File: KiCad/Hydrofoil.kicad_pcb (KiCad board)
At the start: 2 copper layers, 219.6 x 35 mm, 20 parts, among them J1 Conn_01x05_Pin, U1 LM334M, U2 LM334M, U3 ADS1115IDGS

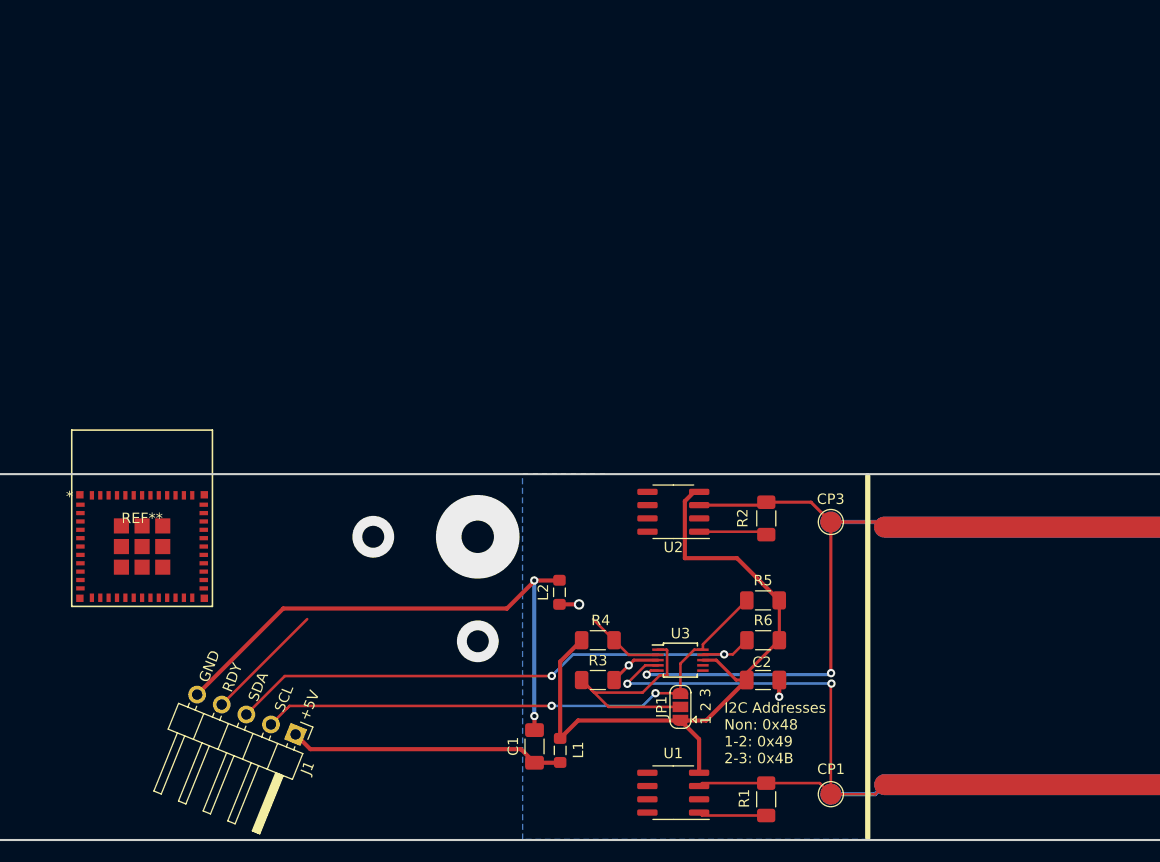
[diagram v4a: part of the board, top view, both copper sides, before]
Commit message: Add level shifters
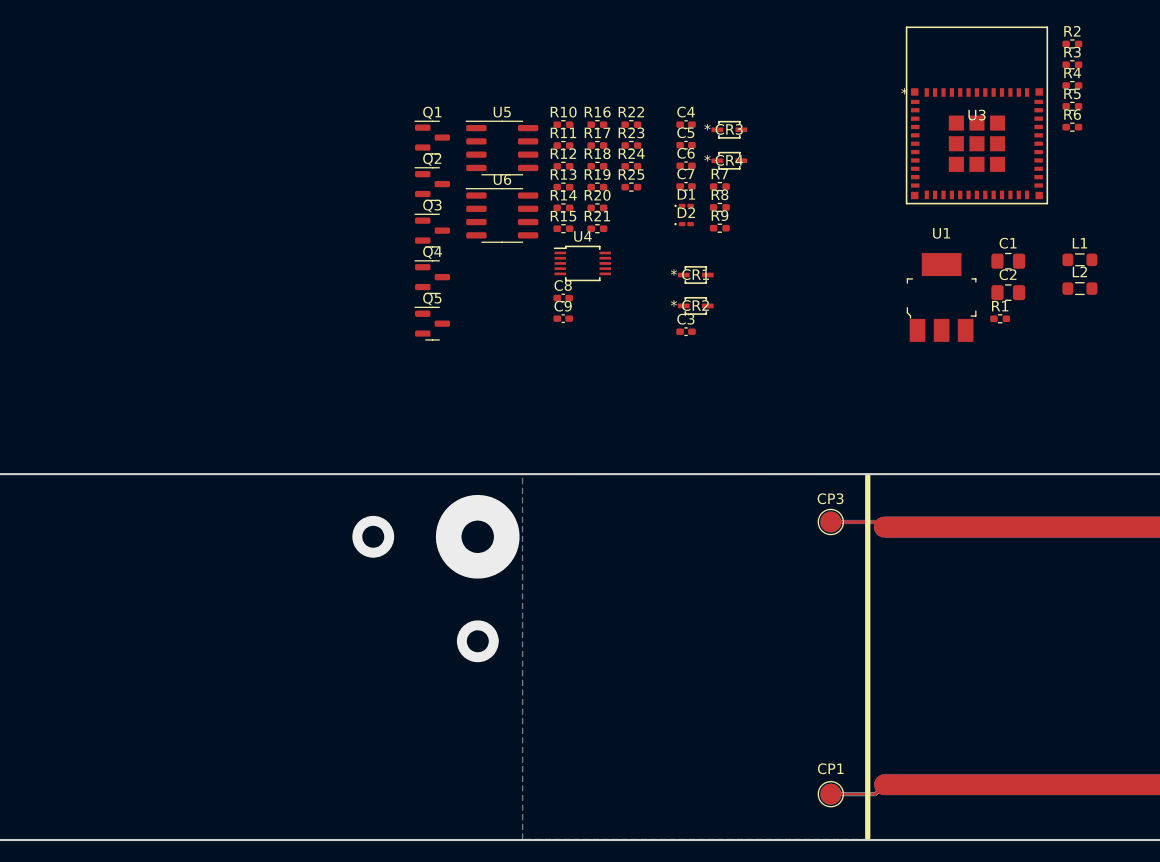
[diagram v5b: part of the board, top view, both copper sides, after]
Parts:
- removed J1: Conn_01x05_Pin, Connector_PinHeader_2.54mm:PinHeader_1x05_P2.54mm_Horizontal
- removed JP1: SolderJumper_3_Open, Jumper:SolderJumper-3_P1.3mm_Open_RoundedPad1.0x1.5mm
- removed REF**: ESP32-C3-MINI-1_EXP, ESP32-C3-MINI-1-N4:ESP32-C3-MINI-1_EXP
- removed U2: LM334M, Package_SO:SOIC-8_3.9x4.9mm_P1.27mm
- added C3: 1u, Capacitor_SMD:C_0402_1005Metric_Pad0.74x0.62mm_HandSolder, F.Cu at (116.8, 57.2)
- added C4: 1u, Capacitor_SMD:C_0402_1005Metric_Pad0.74x0.62mm_HandSolder, F.Cu at (116.8, 37.4)
- added C5: 1u, Capacitor_SMD:C_0402_1005Metric_Pad0.74x0.62mm_HandSolder, F.Cu at (116.8, 39.4)
- added C6: 1u, Capacitor_SMD:C_0402_1005Metric_Pad0.74x0.62mm_HandSolder, F.Cu at (116.8, 41.4)
- added C7: 1u, Capacitor_SMD:C_0402_1005Metric_Pad0.74x0.62mm_HandSolder, F.Cu at (116.8, 43.3)
- added C8: 1u, Capacitor_SMD:C_0402_1005Metric_Pad0.74x0.62mm_HandSolder, F.Cu at (105.0, 54.0)
- added C9: 1u, Capacitor_SMD:C_0402_1005Metric_Pad0.74x0.62mm_HandSolder, F.Cu at (105.0, 56.0)
- added CR1: CUS08F30_H3FT, CUS08F30:USC_TOS, F.Cu at (117.7, 51.8)
- added CR2: CUS08F30_H3FT, CUS08F30:USC_TOS, F.Cu at (117.7, 54.8)
- added CR3: CUS08F30_H3FT, CUS08F30:USC_TOS, F.Cu at (120.9, 37.9)
- added CR4: CUS08F30_H3FT, CUS08F30:USC_TOS, F.Cu at (120.9, 40.9)
- added D1: Green, LED_SMD:LED_0201_0603Metric_Pad0.64x0.40mm_HandSolder, F.Cu at (116.8, 45.2)
- added D2: Red, LED_SMD:LED_0201_0603Metric_Pad0.64x0.40mm_HandSolder, F.Cu at (116.8, 46.9)
- added Q1: BSS138, Package_TO_SOT_SMD:SOT-23, F.Cu at (92.5, 38.7)
- added Q2: BSS138, Package_TO_SOT_SMD:SOT-23, F.Cu at (92.5, 43.1)
- added Q3: BSS138, Package_TO_SOT_SMD:SOT-23, F.Cu at (92.5, 47.6)
- added Q4: BSS138, Package_TO_SOT_SMD:SOT-23, F.Cu at (92.5, 52.0)
- added Q5: BSS138, Package_TO_SOT_SMD:SOT-23, F.Cu at (92.5, 56.5)
- added R10: 10.5, Resistor_SMD:R_0402_1005Metric_Pad0.72x0.64mm_HandSolder, F.Cu at (105.0, 37.4)
- added R11: 10.5k, Resistor_SMD:R_0402_1005Metric_Pad0.72x0.64mm_HandSolder, F.Cu at (105.0, 39.4)
- added R12: 10.5k, Resistor_SMD:R_0402_1005Metric_Pad0.72x0.64mm_HandSolder, F.Cu at (105.0, 41.4)
- added R13: 10.5k, Resistor_SMD:R_0402_1005Metric_Pad0.72x0.64mm_HandSolder, F.Cu at (105.0, 43.4)
- added R14: 150R, Resistor_SMD:R_0402_1005Metric_Pad0.72x0.64mm_HandSolder, F.Cu at (105.0, 45.4)
- added R15: 10.5k, Resistor_SMD:R_0402_1005Metric_Pad0.72x0.64mm_HandSolder, F.Cu at (105.0, 47.4)
- added R16: 10.5k, Resistor_SMD:R_0402_1005Metric_Pad0.72x0.64mm_HandSolder, F.Cu at (108.3, 37.4)
- added R17: 150R, Resistor_SMD:R_0402_1005Metric_Pad0.72x0.64mm_HandSolder, F.Cu at (108.3, 39.4)
- added R18: 10.5k, Resistor_SMD:R_0402_1005Metric_Pad0.72x0.64mm_HandSolder, F.Cu at (108.3, 41.4)
- added R19: 10.5k, Resistor_SMD:R_0402_1005Metric_Pad0.72x0.64mm_HandSolder, F.Cu at (108.3, 43.4)
- added R20: 10.5k, Resistor_SMD:R_0402_1005Metric_Pad0.72x0.64mm_HandSolder, F.Cu at (108.3, 45.4)
- added R21: 10.5k, Resistor_SMD:R_0402_1005Metric_Pad0.72x0.64mm_HandSolder, F.Cu at (108.3, 47.4)
- added R22: 10.5k, Resistor_SMD:R_0402_1005Metric_Pad0.72x0.64mm_HandSolder, F.Cu at (111.5, 37.4)
- added R23: 10.5k, Resistor_SMD:R_0402_1005Metric_Pad0.72x0.64mm_HandSolder, F.Cu at (111.5, 39.4)
- added R24: 10.5k, Resistor_SMD:R_0402_1005Metric_Pad0.72x0.64mm_HandSolder, F.Cu at (111.5, 41.4)
- added R25: 10.5k, Resistor_SMD:R_0402_1005Metric_Pad0.72x0.64mm_HandSolder, F.Cu at (111.5, 43.4)
- added R7: 10.5k, Resistor_SMD:R_0402_1005Metric_Pad0.72x0.64mm_HandSolder, F.Cu at (120.0, 43.3)
- added R8: 1k, Resistor_SMD:R_0402_1005Metric_Pad0.72x0.64mm_HandSolder, F.Cu at (120.0, 45.3)
- added R9: 1k, Resistor_SMD:R_0402_1005Metric_Pad0.72x0.64mm_HandSolder, F.Cu at (120.0, 47.3)
- added U4: ADS1115IDGS, Package_SO:TSSOP-10_3x3mm_P0.5mm, F.Cu at (106.9, 50.7)
- added U5: LM334M, Package_SO:SOIC-8_3.9x4.9mm_P1.27mm, F.Cu at (99.2, 39.7)
- added U6: LM334M, Package_SO:SOIC-8_3.9x4.9mm_P1.27mm, F.Cu at (99.2, 46.1)
- C1, C2: value 1uF -> 10u; footprint Capacitor_SMD:C_1206_3216Metric_Pad1.33x1.80mm_HandSolder -> Capacitor_SMD:C_0805_2012Metric_Pad1.18x1.45mm_HandSolder
- R1, R2: value 150R -> 10.5k; footprint Resistor_SMD:R_1206_3216Metric_Pad1.30x1.75mm_HandSolder -> Resistor_SMD:R_0402_1005Metric_Pad0.72x0.64mm_HandSolder
- R3, R4: value 10k -> 1k; footprint Resistor_SMD:R_1206_3216Metric_Pad1.30x1.75mm_HandSolder -> Resistor_SMD:R_0402_1005Metric_Pad0.72x0.64mm_HandSolder
- R5, R6: value 10k -> 10.5k; footprint Resistor_SMD:R_1206_3216Metric_Pad1.30x1.75mm_HandSolder -> Resistor_SMD:R_0402_1005Metric_Pad0.72x0.64mm_HandSolder
- U1: value LM334M -> LD1117S33CTR; footprint Package_SO:SOIC-8_3.9x4.9mm_P1.27mm -> digikey-footprints:SOT-223
- U3: value ADS1115IDGS -> ESP32-C3-MINI-1-N4; footprint Package_SO:TSSOP-10_3x3mm_P0.5mm -> ESP32-C3-MINI-1-N4:ESP32-C3-MINI-1_EXP
- moved R3 74.3 mm to (153.7, 31.7)
- moved R4 69.8 mm to (153.7, 33.7)
- moved L1 68.4 mm to (154.4, 50.3), turned to 0 degrees
- moved C1 64.9 mm to (147.6, 50.5), turned to 0 degrees
- moved U3 59.3 mm to (144.6, 36.5)
- moved L2 57.6 mm to (154.4, 53.1), turned to 0 degrees
- moved R6 57.3 mm to (153.7, 37.7), turned to 0 degrees
- moved R5 55.8 mm to (153.7, 35.7), turned to 0 degrees
- moved R2 54.0 mm to (153.7, 29.7), turned to 0 degrees
- moved U1 53.9 mm to (141.2, 53.9), turned to 0 degrees
- moved R1 51.1 mm to (146.8, 56.0), turned to 0 degrees
- moved C2 43.9 mm to (147.6, 53.5), turned to 0 degrees
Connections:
- C1 pad 1: /+5Vraw -> /+5V-Logic
- C1 pad 2: /GNDraw -> GND
- C2 pad 1: GND -> +3.3V
- C2 pad 2: +5V -> GND
- CP2 pad 1: GND -> GNDA
- CP4 pad 1: GND -> GNDA
- L1 pad 1: +5V -> +5VA
- L1 pad 2: /+5Vraw -> +5V
- L2 pad 1: GND -> GNDA
- L2 pad 2: /GNDraw -> GND
- R1 pad 1: /SETcur1 -> /+5V-Raw
- R1 pad 2: AIN0 -> Net-(U2-EN)
- R2 pad 1: /SETcur2 -> +3.3V
- R2 pad 2: AIN1 -> Net-(U3-EN)
- R3 pad 1: /ADDR -> +3.3V
- R3 pad 2: GND -> Net-(D1-A)
- R4 pad 1: +5V -> +3.3V
- R4 pad 2: RDY -> Net-(D2-A)
- R5 pad 1: +5V -> +3.3V
- R5 pad 2: SCL -> User-LED
- R6 pad 1: +5V -> +3.3V
- R6 pad 2: SDA -> Input-Boot
- U1 pad 1: /SETcur1 -> GND
- U1 pad 2: AIN0 -> +3.3V
- U1 pad 3: AIN0 -> /+5V-Logic
- U1 pad 4: +5V -> +3.3V
- U3 pad 1: /ADDR -> GND
- U3 pad 10: SCL -> unconnected-(U3-NC-Pad10)
- U3 pad 2: RDY -> GND
- U3 pad 3: GND -> +3.3V
- U3 pad 4: AIN0 -> unconnected-(U3-NC-Pad4)
- U3 pad 5: AIN1 -> Input-Boot
- U3 pad 8: +5V -> Net-(U3-EN)
- U3 pad 9: SDA -> unconnected-(U3-NC-Pad9)
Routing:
- net GND: track 218.3 -> 0.00 mm, vias 3 -> 0
- net GNDA: track 0.00 -> 209.8 mm
- net +5V: track 67.9 -> 0.00 mm
- net /GNDraw: track 54.1 -> 0.00 mm, vias 2 -> 0
- net SDA: track 52.9 -> 0.00 mm, vias 2 -> 0
- net SCL: track 52.4 -> 0.00 mm, vias 2 -> 0
- net AIN0: track 164.5 -> 117.5 mm, vias 2 -> 0
- net AIN1: track 139.2 -> 92.3 mm, vias 2 -> 0
- net /+5Vraw: track 26.4 -> 0.00 mm
- net /ADDR: track 23.2 -> 0.00 mm
- net RDY: track 19.2 -> 0.00 mm
- net /SETcur2: track 6.53 -> 0.00 mm
- net /SETcur1: track 6.53 -> 0.00 mm
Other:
- board text removed: "+5V"
- board text removed: "1"
- board text removed: "2"
- board text removed: "3"
- board text removed: "GND"
- board text removed: "I2C Addresses Non: 0x48 1-2: 0x49 2-3: 0x4B"
- board text removed: "RDY"
- board text removed: "SCL"
- board text removed: "SDA"

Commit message: Change resistor values
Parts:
- added TP3: ~, Connector:Tag-Connect_TC2030-IDC-NL_2x03_P1.27mm_Vertical, F.Cu at (82.1, 38.9)
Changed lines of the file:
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@@
   (net 61 "unconnected-(U4-AIN2-Pad6)")
   (net 62 "unconnected-(U4-AIN3-Pad7)")
+  (net 63 "ESP-En")
   (footprint "LED_SMD:LED_0201_0603Metric_Pad0.64x0.40mm_HandSolder" (layer "F.Cu")
     (at 116.797876 46.93204)
@@
     )
   )
+  (footprint "Connector:Tag-Connect_TC2030-IDC-NL_2x03_P1.27mm_Vertical" (layer "F.Cu")
+    (at 82.118333 38.874349)
+    (descr "Tag-Connect programming header; http://www.tag-connect.com/Materials/TC2030-IDC-NL.pdf")
+    (tags "tag connect programming header pogo pins")
+    (property "Sheetfile" "ESP32-C3-MINI-1-N4.kicad_sch")
+    (property "Sheetname" "ESP32-C3-MINI-1-N4")
+    (attr exclude_from_pos_files)
+    (fp_text reference "TP3" (at 0 2.7) (layer "F.SilkS")
+        (effects (font (size 1 1) (thickness 0.15)))
+    )
+    (fp_text value "~" (at 0 -2.3) (layer "F.Fab")
+        (effects (font (size 1 1) (thickness 0.15)))
+    )
+    (fp_text user "KEEPOUT" (at 0 0) (layer "Cmts.User")
+        (effects (font (size 0.4 0.4) (thickness 0.07)))
+    )
+    (fp_text user "${REFERENCE}" (at 0 0) (layer "F.Fab")
+        (effects (font (size 1 1) (thickness 0.15)))
+    )
+    (fp_line (start -1.905 1.27) (end -1.905 0.635)
+      (stroke (width 0.12) (type solid)) (layer "F.SilkS"))
+    (fp_line (start -1.27 1.27) (end -1.905 1.27)
+      (stroke (width 0.12) (type solid)) (layer "F.SilkS"))
+    (fp_line (start -3.5 -2) (end 3.5 -2)
+      (stroke (width 0.05) (type solid)) (layer "F.CrtYd"))
+    (fp_line (start -3.5 2) (end -3.5 -2)
+      (stroke (width 0.05) (type solid)) (layer "F.CrtYd"))
+    (fp_line (start 3.5 -2) (end 3.5 2)
+      (stroke (width 0.05) (type solid)) (layer "F.CrtYd"))
+    (fp_line (start 3.5 2) (end -3.5 2)
+      (stroke (width 0.05) (type solid)) (layer "F.CrtYd"))
+    (pad "" np_thru_hole circle (at -2.54 0) (size 0.9906 0.9906) (drill 0.9906) (layers "*.Cu" "*.Mask"))
+    (pad "" np_thru_hole circle (at 2.54 -1.016) (size 0.9906 0.9906) (drill 0.9906) (layers "*.Cu" "*.Mask"))
+    (pad "" np_thru_hole circle (at 2.54 1.016) (size 0.9906 0.9906) (drill 0.9906) (layers "*.Cu" "*.Mask"))
+    (pad "1" connect circle (at -1.27 0.635) (size 0.7874 0.7874) (layers "F.Cu" "F.Mask")
+      (net 63 "ESP-En") (pintype "input"))
+    (pad "2" connect circle (at -1.27 -0.635) (size 0.7874 0.7874) (layers "F.Cu" "F.Mask")
+      (net 12 "+5V-Prog") (pintype "power_in"))
+    (pad "3" connect circle (at 0 0.635) (size 0.7874 0.7874) (layers "F.Cu" "F.Mask")
+      (net 56 "ESP-Tx") (pintype "input"))
+    (pad "4" connect circle (at 0 -0.635) (size 0.7874 0.7874) (layers "F.Cu" "F.Mask")
+      (net 3 "GND") (pintype "power_in"))
+    (pad "5" connect circle (at 1.27 0.635) (size 0.7874 0.7874) (layers "F.Cu" "F.Mask")
+      (net 55 "ESP-Rx") (pintype "input"))
+    (pad "6" connect circle (at 1.27 -0.635) (size 0.7874 0.7874) (layers "F.Cu" "F.Mask")
+      (net 14 "ESP-Boot") (pintype "output"))
+    (zone (net 0) (net_name "") (layer "F.Cu") (hatch full 0.508)
+      (connect_pads (clearance 0))
+      (min_thickness 0.254) (filled_areas_thickness no)
+      (keepout (tracks allowed) (vias not_allowed) (pads allowed) (copperpour not_allowed) (footprints not_allowed))
+      (fill (thermal_gap 0.508) (thermal_bridge_width 0.508))
+      (polygon
+        (pts
+          (xy 83.388333 38.239349)
+          (xy 80.848333 38.239349)
+          (xy 80.848333 39.509349)
+          (xy 83.388333 39.509349)
+        )
+      )
+    )
+  )
   (footprint "Resistor_SMD:R_0402_1005Metric_Pad0.72x0.64mm_HandSolder" (layer "F.Cu")
     (at 153.723374 31.686694)
@@
         (effects (font (size 1 1) (thickness 0.15)))
     )
+    (fp_text user "*" (at -6.9414 -2.0759 unlocked) (layer "F.SilkS")
+        (effects (font (size 1 1) (thickness 0.15)))
+    )
     (fp_text user "*" (at -6.9414 -2.0759) (layer "F.SilkS")
         (effects (font (size 1 1) (thickness 0.15)))
     )
-    (fp_text user "*" (at -6.9414 -2.0759 unlocked) (layer "F.SilkS")
+    (fp_text user "*" (at -5.2396 -1.6949 unlocked) (layer "F.Fab")
         (effects (font (size 1 1) (thickness 0.15)))
     )
@@
         (effects (font (size 1 1) (thickness 0.15)))
     )
-    (fp_text user "*" (at -5.2396 -1.6949 unlocked) (layer "F.Fab")
-        (effects (font (size 1 1) (thickness 0.15)))
-    )

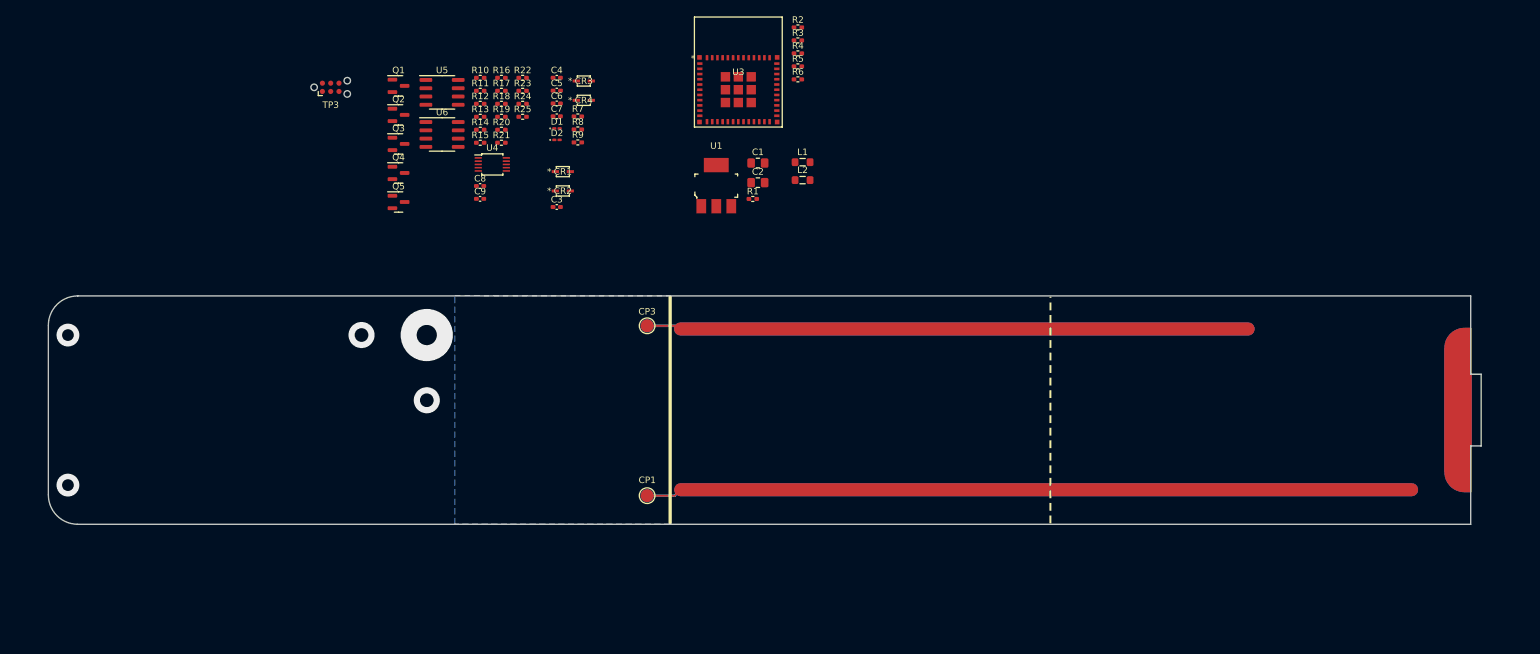
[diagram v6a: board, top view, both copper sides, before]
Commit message: Change reverse polarity protection, start the PCB design
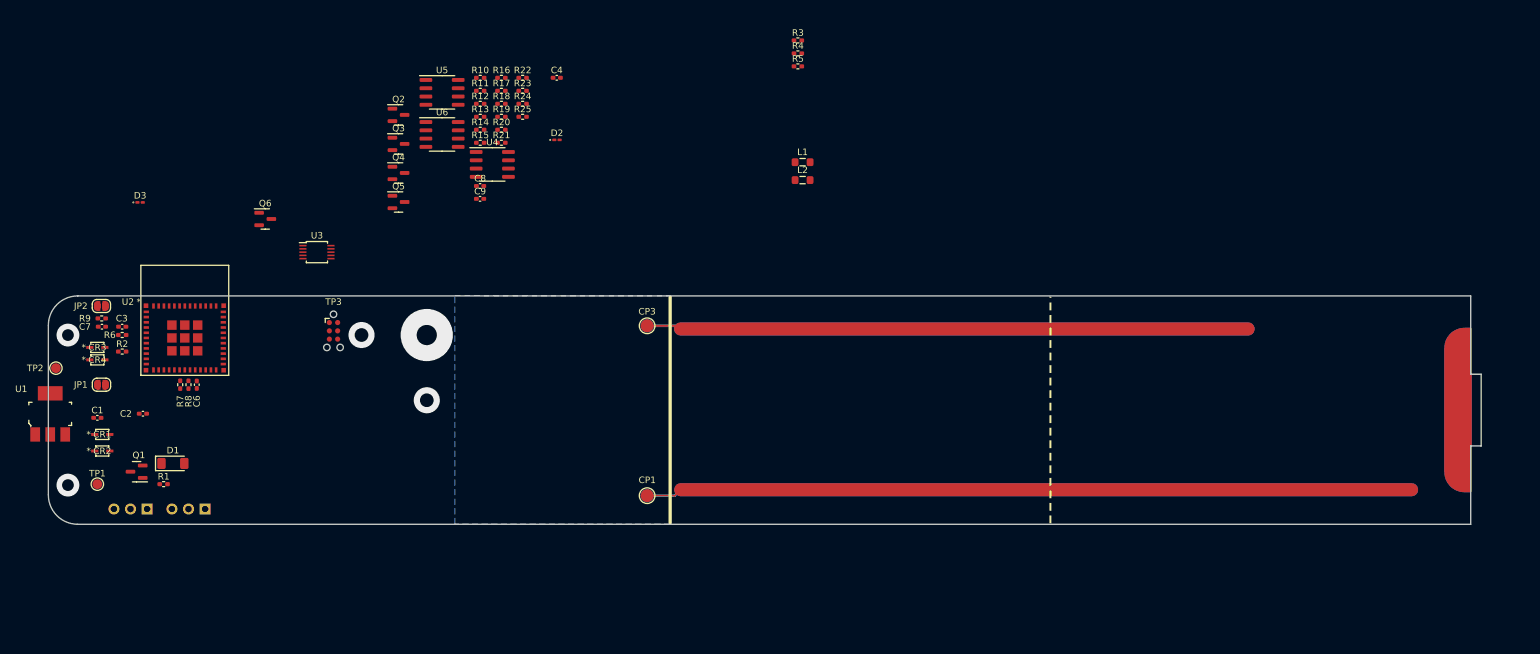
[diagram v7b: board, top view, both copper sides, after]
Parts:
- removed C5: 1u, Capacitor_SMD:C_0402_1005Metric_Pad0.74x0.62mm_HandSolder
- added D3: Red, LED_SMD:LED_0201_0603Metric_Pad0.64x0.40mm_HandSolder, F.Cu at (52.9, 56.5)
- added J1: Conn_01x03_Pin, Custom_Footprints:Solder_Connector, F.Cu at (51.4, 103.5)
- added J2: Conn_01x03_Pin, Custom_Footprints:Solder_Connector, F.Cu at (60.3, 103.5)
- added JP1: Jumper_2_Open, Jumper:SolderJumper-2_P1.3mm_Open_RoundedPad1.0x1.5mm, F.Cu at (47.0, 84.5)
- added JP2: Jumper_2_Open, Jumper:SolderJumper-2_P1.3mm_Open_RoundedPad1.0x1.5mm, F.Cu at (47.0, 72.4)
- added Q6: BSS138, Package_TO_SOT_SMD:SOT-23, F.Cu at (72.1, 59.1)
- added TP1: TestPoint, TestPoint:TestPoint_Pad_D1.5mm, F.Cu at (46.4, 99.7)
- added TP2: TestPoint, TestPoint:TestPoint_Pad_D1.5mm, F.Cu at (40.0, 81.9)
- added U2: ESP32-C3-MINI-1-N4, ESP32-C3-MINI-1-N4:ESP32-C3-MINI-1_EXP, F.Cu at (59.8, 74.6)
- C1, C2: footprint Capacitor_SMD:C_0805_2012Metric_Pad1.18x1.45mm_HandSolder -> Capacitor_SMD:C_0402_1005Metric_Pad0.74x0.62mm_HandSolder
- C3: value 1u -> 10u
- D1: value Green -> BZV55B7V5; footprint LED_SMD:LED_0201_0603Metric_Pad0.64x0.40mm_HandSolder -> Diode_SMD:D_MiniMELF
- D2: value Red -> Green
- Q1: value BSS138 -> AO3413
- R1: value 10.5k -> 100k
- R10: value 10.5 -> 10k
- R11, R12, R13, R15, R16, R18, R19, R2, R20, R21, R22, R23, R24, R25, R5, R6, R7: value 10.5k -> 10k
- U3: value ESP32-C3-MINI-1-N4 -> ADS1115IDGS; footprint ESP32-C3-MINI-1-N4:ESP32-C3-MINI-1_EXP -> Package_SO:TSSOP-10_3x3mm_P0.5mm
- U4: value ADS1115IDGS -> LM334M; footprint Package_SO:TSSOP-10_3x3mm_P0.5mm -> Package_SO:SOIC-8_3.9x4.9mm_P1.27mm
- moved R2 114.9 mm to (50.2, 79.4)
- moved R6 110.7 mm to (50.2, 76.8)
- moved C1 108.5 mm to (46.4, 89.5)
- moved U1 107.9 mm to (39.1, 88.9)
- moved C2 100.7 mm to (53.3, 88.9)
- moved R1 100.3 mm to (56.5, 99.7)
- moved CR3 85.0 mm to (46.4, 78.7)
- moved CR4 84.5 mm to (46.4, 80.6)
- moved CR1 81.3 mm to (47.1, 92.1)
- moved CR2 81.1 mm to (47.1, 94.6)
- moved D1 78.1 mm to (57.9, 96.5)
- moved R9 77.8 mm to (47.0, 74.3)
- moved C7 76.8 mm to (47.1, 75.6)
- moved R7 73.5 mm to (59.1, 84.5), turned to 90 degrees
- moved Q1 71.5 mm to (52.4, 97.8), turned to 180 degrees
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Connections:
- C2 pad 1: +3.3V -> +5V
- C3 pad 1: +5V -> +3.3V
- C4 pad 1: Net-(U3-EN) -> Net-(U2-EN)
- D1 pad 1: GND -> +5V
- D2 pad 1: User-LED -> GND
- Q1 pad 1: +3.3V -> Net-(D1-A)
- Q1 pad 2: Ready-LV -> +5V
- Q1 pad 3: Ready-HV -> /+5V-Raw
- Q2 pad 2: SDA-LV -> Ready-LV
- Q2 pad 3: SDA-HV -> Ready-HV
- Q3 pad 2: SCL-LV -> SDA-LV
- Q3 pad 3: SCL-HV -> SDA-HV
- Q4 pad 2: PWM-In-LV -> SCL-LV
- Q4 pad 3: PWM-In-HV -> SCL-HV
- Q5 pad 2: PWM-Out-LV -> PWM-In-LV
- Q5 pad 3: PWM-Out-HV -> PWM-In-HV
- R1 pad 1: /+5V-Raw -> Net-(D1-A)
- R1 pad 2: Net-(U2-EN) -> GND
- R10 pad 1: Net-(U4-ADDR) -> Net-(U3-ADDR)
- R15 pad 1: +3.3V -> unconnected-(R15-Pad1)
- R15 pad 2: Ready-LV -> unconnected-(R15-Pad2)
- R16 pad 2: SDA-LV -> Ready-LV
- R2 pad 2: Net-(U3-EN) -> Net-(U2-EN)
- R3 pad 2: Net-(D1-A) -> Net-(D2-A)
- R4 pad 2: Net-(D2-A) -> Net-(D3-A)
- U3 pad 1: GND -> Net-(U3-ADDR)
- U3 pad 10: unconnected-(U3-NC-Pad10) -> SCL-HV
- U3 pad 2: GND -> Ready-HV
- U3 pad 3: +3.3V -> GNDA
- U3 pad 4: unconnected-(U3-NC-Pad4) -> AIN0
- U3 pad 5: Input-Boot -> AIN1
- U3 pad 8: Net-(U3-EN) -> +5VA
- U3 pad 9: unconnected-(U3-NC-Pad9) -> SDA-HV
- U4 pad 1: Net-(U4-ADDR) -> /ADS1115-ADC/SETcur1
- U4 pad 2: Ready-HV -> AIN0
- U4 pad 3: GNDA -> AIN0
- U4 pad 4: AIN0 -> +5VA
- U4 pad 5: AIN1 -> (no net)
- U4 pad 6: unconnected-(U4-AIN2-Pad6) -> AIN0
- U4 pad 7: unconnected-(U4-AIN3-Pad7) -> AIN0
- U4 pad 8: +5VA -> (no net)
- U5 pad 1: /ADS1115-ADC/SETcur1 -> /ADS1115-ADC/SETcur2
- U5 pad 2: AIN0 -> AIN1
- U5 pad 3: AIN0 -> AIN1
- U5 pad 6: AIN0 -> AIN1
- U5 pad 7: AIN0 -> AIN1
